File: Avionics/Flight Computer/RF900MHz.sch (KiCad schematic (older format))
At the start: 49 parts, among them J4 734120110, U1 CC1310F128RGZR, U2 CC1190RGVR, Y3 XRCGB24M000F2P00R0

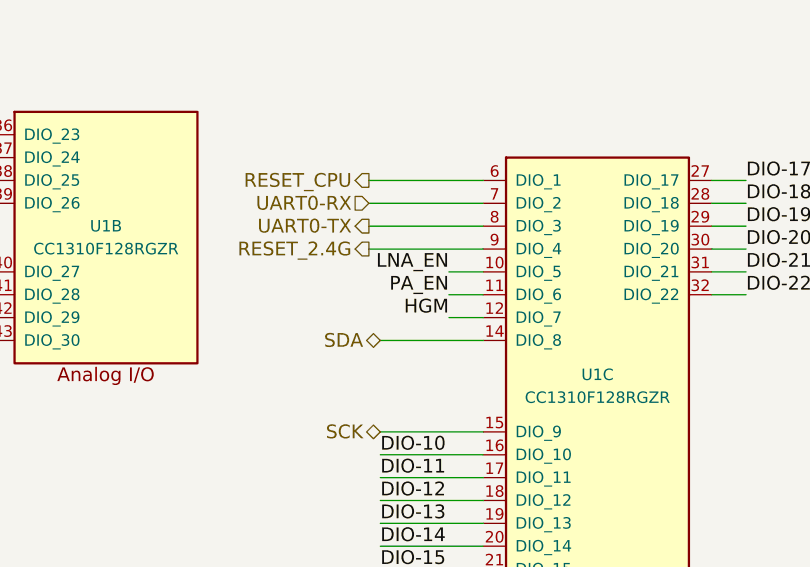
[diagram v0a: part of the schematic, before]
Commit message: Swapped some pins to make routing easier.
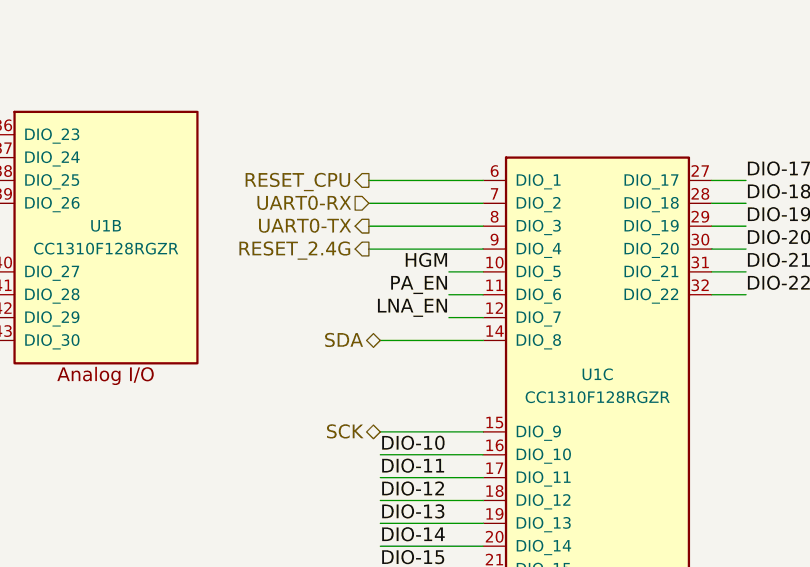
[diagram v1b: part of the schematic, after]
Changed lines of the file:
@@
 Text Label 4050 5800 2    60   ~ 0
 PA_EN
+Text Label 4050 5900 2    60   ~ 0
+LNA_EN
 Text Label 4050 5700 2    60   ~ 0
-LNA_EN
-Text Label 4050 5900 2    60   ~ 0
 HGM
 Wire Wire Line

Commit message: Finished routing and DRC check.
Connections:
- wire segments 124 -> 130
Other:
- moved on the sheet: C17, R9

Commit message: Added LEDs
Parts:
- R4: value 3.35 -> 3.3k
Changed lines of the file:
@@
 EESchema Schematic File Version 2
-LIBS:Flight Computer-rescue
 LIBS:device
 LIBS:rfcom
@@
 $EndComp
 $Comp
-L GND #PWR038
+L GND #PWR046
 U 1 1 58AA1A95
 P 10900 2500
-F 0 "#PWR038" H 10900 2250 50  0001 C CNN
+F 0 "#PWR046" H 10900 2250 50  0001 C CNN
 F 1 "GND" H 10900 2350 50  0000 C CNN
 F 2 "" H 10900 2500 50  0001 C CNN
@@
 $EndComp
 $Comp
-L GND #PWR039
+L GND #PWR047
 U 1 1 58AA3683
 P 10050 2700
-F 0 "#PWR039" H 10050 2450 50  0001 C CNN
+F 0 "#PWR047" H 10050 2450 50  0001 C CNN
 F 1 "GND" H 10050 2550 50  0000 C CNN
 F 2 "" H 10050 2700 50  0001 C CNN
@@
 $EndComp
 $Comp
-L GND #PWR040
+L GND #PWR048
 U 1 1 58AA36BB
 P 9550 2700
-F 0 "#PWR040" H 9550 2450 50  0001 C CNN
+F 0 "#PWR048" H 9550 2450 50  0001 C CNN
 F 1 "GND" H 9550 2550 50  0000 C CNN
 F 2 "" H 9550 2700 50  0001 C CNN
@@
 $EndComp
 $Comp
-L GND #PWR041
+L GND #PWR049
 U 1 1 58AA36F3
 P 9000 2700
-F 0 "#PWR041" H 9000 2450 50  0001 C CNN
+F 0 "#PWR049" H 9000 2450 50  0001 C CNN
 F 1 "GND" H 9000 2550 50  0000 C CNN
 F 2 "" H 9000 2700 50  0001 C CNN
@@
 $EndComp
 $Comp
-L GND #PWR042
+L GND #PWR050
 U 1 1 58AA409E
 P 7050 3450
-F 0 "#PWR042" H 7050 3200 50  0001 C CNN
+F 0 "#PWR050" H 7050 3200 50  0001 C CNN
 F 1 "GND" H 7050 3300 50  0000 C CNN
 F 2 "" H 7050 3450 50  0001 C CNN
@@
 $EndComp
 $Comp
-L GND #PWR043
+L GND #PWR051
 U 1 1 58AA431F
 P 3100 3150
-F 0 "#PWR043" H 3100 2900 50  0001 C CNN
+F 0 "#PWR051" H 3100 2900 50  0001 C CNN
 F 1 "GND" H 3100 3000 50  0000 C CNN
 F 2 "" H 3100 3150 50  0001 C CNN
@@
 $EndComp
 $Comp
-L GND #PWR044
+L GND #PWR052
 U 1 1 58AABD29
 P 7250 5150
-F 0 "#PWR044" H 7250 4900 50  0001 C CNN
+F 0 "#PWR052" H 7250 4900 50  0001 C CNN
 F 1 "GND" H 7250 5000 50  0000 C CNN
 F 2 "" H 7250 5150 50  0001 C CNN
@@
 $EndComp
 $Comp
-L GND #PWR045
+L GND #PWR053
 U 1 1 58AAF7AF
 P 6700 1500
-F 0 "#PWR045" H 6700 1250 50  0001 C CNN
+F 0 "#PWR053" H 6700 1250 50  0001 C CNN
 F 1 "GND" H 6700 1350 50  0000 C CNN
 F 2 "" H 6700 1500 50  0001 C CNN
@@
 Shielded Area
 $Comp
-L GND #PWR046
+L GND #PWR054
 U 1 1 58AB0BB7
 P 6350 3450
-F 0 "#PWR046" H 6350 3200 50  0001 C CNN
+F 0 "#PWR054" H 6350 3200 50  0001 C CNN
 F 1 "GND" H 6350 3300 50  0000 C CNN
 F 2 "" H 6350 3450 50  0001 C CNN
@@
 $EndComp
 $Comp
-L GND #PWR047
+L GND #PWR055
 U 1 1 58AB2D32
 P 9950 1500
-F 0 "#PWR047" H 9950 1250 50  0001 C CNN
+F 0 "#PWR055" H 9950 1250 50  0001 C CNN
 F 1 "GND" H 9950 1350 50  0000 C CNN
 F 2 "" H 9950 1500 50  0001 C CNN
@@
 VDDS_CC1310
 $Comp
-L GND #PWR048
+L GND #PWR056
 U 1 1 58AE74D7
 P 4000 3300
-F 0 "#PWR048" H 4000 3050 50  0001 C CNN
+F 0 "#PWR056" H 4000 3050 50  0001 C CNN
 F 1 "GND" H 4000 3150 50  0000 C CNN
 F 2 "" H 4000 3300 50  0001 C CNN
@@
 $EndComp
 $Comp
-L GND #PWR049
+L GND #PWR057
 U 1 1 58AF2937
 P 8050 5150
-F 0 "#PWR049" H 8050 4900 50  0001 C CNN
+F 0 "#PWR057" H 8050 4900 50  0001 C CNN
 F 1 "GND" H 8050 5000 50  0000 C CNN
 F 2 "" H 8050 5150 50  0001 C CNN
@@
 Connection ~ 8050 4800
 $Comp
-L GND #PWR050
+L GND #PWR058
 U 1 1 58AF2A67
 P 8400 5150
-F 0 "#PWR050" H 8400 4900 50  0001 C CNN
+F 0 "#PWR058" H 8400 4900 50  0001 C CNN
 F 1 "GND" H 8400 5000 50  0000 C CNN
 F 2 "" H 8400 5150 50  0001 C CNN
@@
 $EndComp
 $Comp
-L GND #PWR051
+L GND #PWR059
 U 1 1 58AF2BB0
 P 8750 5150
-F 0 "#PWR051" H 8750 4900 50  0001 C CNN
+F 0 "#PWR059" H 8750 4900 50  0001 C CNN
 F 1 "GND" H 8750 5000 50  0000 C CNN
 F 2 "" H 8750 5150 50  0001 C CNN
@@
 $EndComp
 $Comp
-L GND #PWR052
+L GND #PWR060
 U 1 1 58AF2C21
 P 9100 5150
-F 0 "#PWR052" H 9100 4900 50  0001 C CNN
+F 0 "#PWR060" H 9100 4900 50  0001 C CNN
 F 1 "GND" H 9100 5000 50  0000 C CNN
 F 2 "" H 9100 5150 50  0001 C CNN
@@
 	9600 4800 9600 4850
 $Comp
-L GND #PWR053
+L GND #PWR061
 U 1 1 58AF39C7
 P 9600 5150
-F 0 "#PWR053" H 9600 4900 50  0001 C CNN
+F 0 "#PWR061" H 9600 4900 50  0001 C CNN
 F 1 "GND" H 9600 5000 50  0000 C CNN
 F 2 "" H 9600 5150 50  0001 C CNN
@@
 Connection ~ 2900 1150
 $Comp
-L GND #PWR054
+L GND #PWR062
 U 1 1 58AF55B9
 P 2500 1550
-F 0 "#PWR054" H 2500 1300 50  0001 C CNN
+F 0 "#PWR062" H 2500 1300 50  0001 C CNN
 F 1 "GND" H 2500 1400 50  0000 C CNN
 F 2 "" H 2500 1550 50  0001 C CNN
@@
 Connection ~ 1850 1150
 $Comp
-L GND #PWR055
+L GND #PWR063
 U 1 1 58AF6EFE
 P 1850 1550
-F 0 "#PWR055" H 1850 1300 50  0001 C CNN
+F 0 "#PWR063" H 1850 1300 50  0001 C CNN
 F 1 "GND" H 1850 1400 50  0000 C CNN
 F 2 "" H 1850 1550 50  0001 C CNN
@@
 $EndComp
 $Comp
-L GND #PWR056
+L GND #PWR064
 U 1 1 58AF6F78
 P 1500 1550
-F 0 "#PWR056" H 1500 1300 50  0001 C CNN
+F 0 "#PWR064" H 1500 1300 50  0001 C CNN
 F 1 "GND" H 1500 1400 50  0000 C CNN
 F 2 "" H 1500 1550 50  0001 C CNN
@@
 PIN 48
 $Comp
-L GND #PWR057
+L GND #PWR065
 U 1 1 58AF9836
 P 8050 1100
-F 0 "#PWR057" H 8050 850 50  0001 C CNN
+F 0 "#PWR065" H 8050 850 50  0001 C CNN
 F 1 "GND" H 8050 950 50  0000 C CNN
 F 2 "" H 8050 1100 50  0001 C CNN
@@
 $EndComp
 $Comp
-L GND #PWR058
+L GND #PWR066
 U 1 1 58AF99F1
 P 8500 1100
-F 0 "#PWR058" H 8500 850 50  0001 C CNN
+F 0 "#PWR066" H 8500 850 50  0001 C CNN
 F 1 "GND" H 8500 950 50  0000 C CNN
 F 2 "" H 8500 1100 50  0001 C CNN
@@
 $EndComp
 $Comp
-L GND #PWR059
+L GND #PWR067
 U 1 1 58AF9A68
 P 8950 1100
-F 0 "#PWR059" H 8950 850 50  0001 C CNN
+F 0 "#PWR067" H 8950 850 50  0001 C CNN
 F 1 "GND" H 8950 950 50  0000 C CNN
 F 2 "" H 8950 1100 50  0001 C CNN
@@
 Connection ~ 7800 1150
 $Comp
-L GND #PWR060
+L GND #PWR068
 U 1 1 58AFAEF6
 P 7550 1450
-F 0 "#PWR060" H 7550 1200 50  0001 C CNN
+F 0 "#PWR068" H 7550 1200 50  0001 C CNN
 F 1 "GND" H 7550 1300 50  0000 C CNN
 F 2 "" H 7550 1450 50  0001 C CNN
@@
 VDD_CC1190
 $Comp
-L GND #PWR061
+L GND #PWR069
 U 1 1 58AFDB01
 P 8000 6050
-F 0 "#PWR061" H 8000 5800 50  0001 C CNN
+F 0 "#PWR069" H 8000 5800 50  0001 C CNN
 F 1 "GND" H 8000 5900 50  0000 C CNN
 F 2 "" H 8000 6050 50  0001 C CNN
@@
 Connection ~ 8000 5750
 $Comp
-L +3.3V #PWR062
+L +3.3V #PWR070
 U 1 1 58ABA1EC
 P 6500 4700
-F 0 "#PWR062" H 6550 4750 50  0001 C CNN
+F 0 "#PWR070" H 6550 4750 50  0001 C CNN
 F 1 "+3.3V" H 6515 4873 50  0000 C CNN
 F 2 "" H -150 250 50  0001 C CNN
@@
 $EndComp
 $Comp
-L GND #PWR063
+L GND #PWR071
 U 1 1 58B338EF
 P 5700 2650
-F 0 "#PWR063" H 5700 2400 50  0001 C CNN
+F 0 "#PWR071" H 5700 2400 50  0001 C CNN
 F 1 "GND" H 5700 2500 50  0000 C CNN
 F 2 "" H 5700 2650 50  0001 C CNN
@@
 Connection ~ 5700 2300
 $Comp
-L GND #PWR064
+L GND #PWR072
 U 1 1 58B33B39
 P 5200 2400
-F 0 "#PWR064" H 5200 2150 50  0001 C CNN
+F 0 "#PWR072" H 5200 2150 50  0001 C CNN
 F 1 "GND" H 5200 2250 50  0000 C CNN
 F 2 "" H 5200 2400 50  0001 C CNN
@@
 $EndComp
 $Comp
-L GND #PWR065
+L GND #PWR073
 U 1 1 58B33E63
 P 4600 2400
-F 0 "#PWR065" H 4600 2150 50  0001 C CNN
+F 0 "#PWR073" H 4600 2150 50  0001 C CNN
 F 1 "GND" H 4600 2250 50  0000 C CNN
 F 2 "" H 4600 2400 50  0001 C CNN
@@
 P 6350 3200
 F 0 "R4" V 6300 3350 50  0000 C CNN
-F 1 "3.35" V 6350 3200 50  0000 C CNN
+F 1 "3.3k" V 6350 3200 50  0000 C CNN
 F 2 "Resistors_SMD:R_0402" V 1450 2200 50  0001 C CNN
 F 3 "" V 1730 2200 50  0001 C CNN
@@
 $EndComp
 $Comp
-L GND #PWR066
+L GND #PWR074
 U 1 1 58B9C757
 P 1950 3700
-F 0 "#PWR066" H 1950 3450 50  0001 C CNN
+F 0 "#PWR074" H 1950 3450 50  0001 C CNN
 F 1 "GND" H 1950 3550 50  0000 C CNN
 F 2 "" H 1950 3700 50  0001 C CNN
@@
 $EndComp
 $Comp
-L GND #PWR067
+L GND #PWR075
 U 1 1 58C2B89B
 P 1050 2250
-F 0 "#PWR067" H 1100 2300 50  0001 C CNN
+F 0 "#PWR075" H 1100 2300 50  0001 C CNN
 F 1 "GND" H 1055 2077 50  0000 C CNN
 F 2 "" H -5750 -1500 50  0001 C CNN
@@
 $EndComp
 $Comp
-L +3.3V #PWR068
+L +3.3V #PWR076
 U 1 1 58C2B8B0
 P 1050 1550
-F 0 "#PWR068" H 1100 1600 50  0001 C CNN
+F 0 "#PWR076" H 1100 1600 50  0001 C CNN
 F 1 "+3.3V" H 1050 1700 50  0000 C CNN
 F 2 "" H -6300 -3250 50  0001 C CNN
@@
 	3750 6000 4200 6000
 $Comp
-L PWR_FLAG #FLG069
+L PWR_FLAG #FLG077
 U 1 1 58BE7A76
 P 6550 1100
-F 0 "#FLG069" H 150 175 50  0001 C CNN
+F 0 "#FLG077" H 150 175 50  0001 C CNN
 F 1 "PWR_FLAG" H 6550 1274 50  0000 C CNN
 F 2 "" H 150 100 50  0001 C CNN
@@
 Connection ~ 6750 1200
 $Comp
-L PWR_FLAG #FLG070
+L PWR_FLAG #FLG078
 U 1 1 58BE7D62
 P 7200 950
-F 0 "#FLG070" H 800 25  50  0001 C CNN
+F 0 "#FLG078" H 800 25  50  0001 C CNN
 F 1 "PWR_FLAG" V 7200 1078 50  0000 L CNN
 F 2 "" H 800 -50 50  0001 C CNN
@@
 	7200 1150 7200 950
 $Comp
-L PWR_FLAG #FLG071
+L PWR_FLAG #FLG079
 U 1 1 58BE8C3A
 P 7400 1550
-F 0 "#FLG071" H 1000 625 50  0001 C CNN
+F 0 "#FLG079" H 1000 625 50  0001 C CNN
 F 1 "PWR_FLAG" H 7400 1723 50  0000 C CNN
 F 2 "" H 1000 550 50  0001 C CNN
@@
 Connection ~ 7150 1600
 $Comp
-L PWR_FLAG #FLG072
+L PWR_FLAG #FLG080
 U 1 1 58BE99E2
 P 3000 1150
-F 0 "#FLG072" H -1350 275 50  0001 C CNN
+F 0 "#FLG080" H -1350 275 50  0001 C CNN
 F 1 "PWR_FLAG" H 3000 1324 50  0000 C CNN
 F 2 "" H -1350 200 50  0001 C CNN
@@
 $EndComp
 $Comp
-L PWR_FLAG #FLG073
+L PWR_FLAG #FLG081
 U 1 1 58BECF0F
 P 9750 4800
-F 0 "#FLG073" H 5400 3925 50  0001 C CNN
+F 0 "#FLG081" H 5400 3925 50  0001 C CNN
 F 1 "PWR_FLAG" H 9750 4974 50  0000 C CNN
 F 2 "" H 5400 3850 50  0001 C CNN
@@
 Connection ~ 9600 4800
 $Comp
-L PWR_FLAG #FLG074
+L PWR_FLAG #FLG082
 U 1 1 58BED565
 P 8950 5750
-F 0 "#FLG074" H 4600 4875 50  0001 C CNN
+F 0 "#FLG082" H 4600 4875 50  0001 C CNN
 F 1 "PWR_FLAG" H 8950 5924 50  0000 C CNN
 F 2 "" H 4600 4800 50  0001 C CNN

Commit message: Changed LED configuration, added smart driver chip to let all the CPUs access it..
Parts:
- added D6: LED-0603-RED, LEDs:LED_0603, symbol LED
- added R47: 1k, Resistors_SMD:R_0402, symbol R
- C1, C13, C14, C15, C17, C18, C2, C20, C21, C24, C25, C26, C27, C29, C5, C6, C66, C67, C7, C88, C9, R1, R2, R3, R35, R4, R9: Voltage 50V -> 16V
- C28, C4: footprint Capacitors_SMD:C_0603 -> Capacitors_SMD:C_0402; Package 0603 -> 0402; Type X7R -> X5R; Voltage 50V -> 16V
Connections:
- wire segments 130 -> 133

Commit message: Built outputs and added manufacturing part numbers to make BOM search easier.
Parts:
- C1, C2: value 0.1 -> 0.1u
- C13, C21, C9: value 47p -> GRM1555C1H470FA01D
- C15, C17, C18, C26, C66, C67: value 12p -> GRM1555C1H120GA01D
- C16: value 2.2u -> EMK107BJ225KA-T
- C19, C3, C30: value 22u -> EMK212BBJ226MG-T
- C5: value 3.3p -> GJM1555C1H3R3CB01D
- C6: value 7.5p -> GJM1555C1H7R5CB01D
- L1, L14: value 22n -> CIH10T22NJNC
- L12, L18: value 10n -> LQG15HN9N1J02D
- L13, L3: value 2.2n -> HK10052N2S-T
- L4: value 9.1n -> LQG15HN9N1J02D
- L8: value 6.8u -> BRL1608T6R8M; footprint Inductors_SMD:L_0402 -> Inductors_SMD:L_0603
